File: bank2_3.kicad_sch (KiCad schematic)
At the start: 1 part, among them U1 ECP5-BGA256

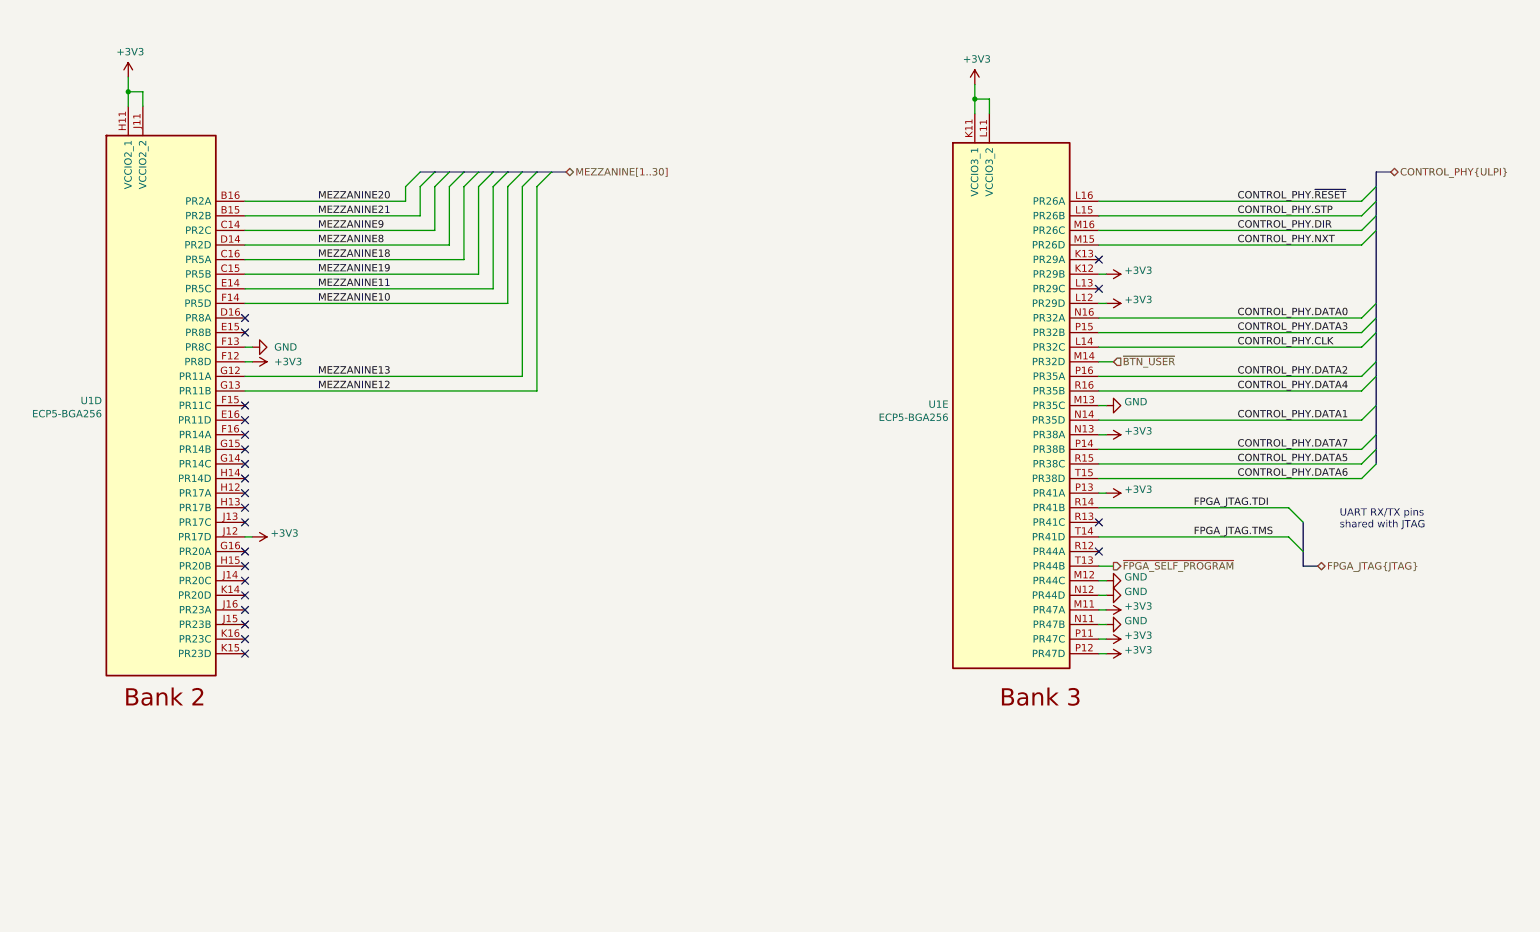
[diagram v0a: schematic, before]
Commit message: Add radio transceiver
Remove Cynthion-specific features
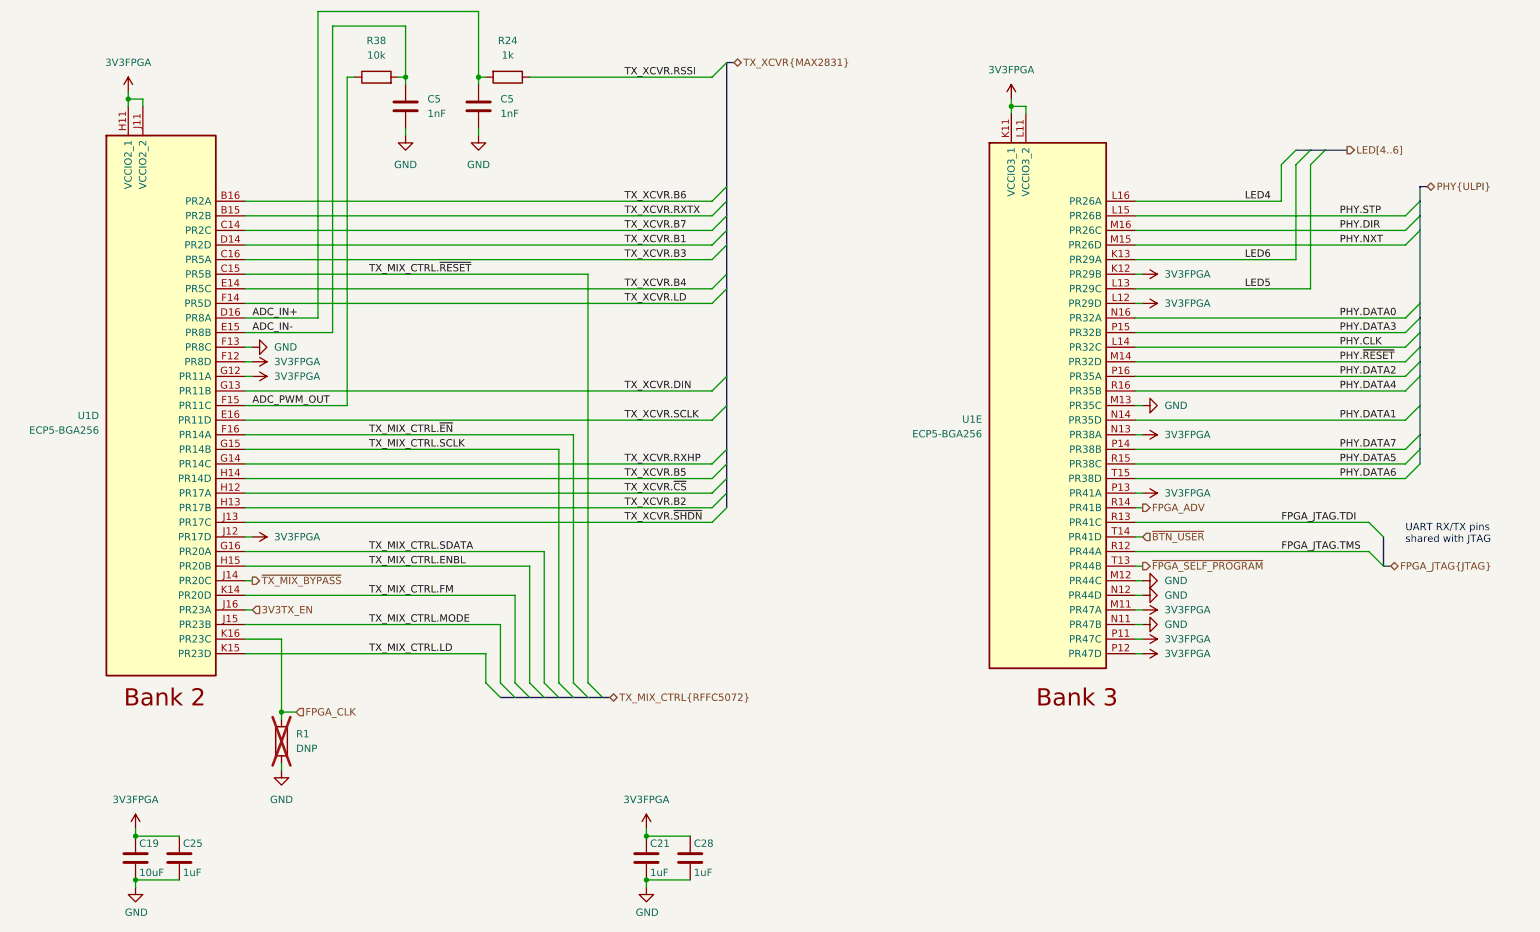
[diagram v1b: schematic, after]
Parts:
- added C19: 10uF, Capacitor_SMD:C_0603_1608Metric, symbol Device:C
- added C21, C25, C28: 1uF, Capacitor_SMD:C_0402_1005Metric, symbol Device:C
- added C5 (x2): 1nF, Capacitor_SMD:C_0201_0603Metric, symbol Device:C
- added R1: DNP, Resistor_SMD:R_0402_1005Metric, symbol Device:R
- added R24: 1k, Resistor_SMD:R_0402_1005Metric, symbol Device:R
- added R38: 10k, Resistor_SMD:R_0402_1005Metric, symbol Device:R
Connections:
- net MEZZANINE13 is gone; now on net 3V3FPGA: U1.G12 (PR11A)
- net FPGA_JTAG.TDI: now also U1.R13 (PR41C); no longer U1.R14 (PR41B)
- net FPGA_JTAG.TMS: now also U1.R12 (PR44A); no longer U1.T14 (PR41D)
- net GND: now also C19.2, C21.2, C25.2, C28.2, C5.2, C5.2, R1.2
- net ~{BTN_USER}: now also U1.T14 (PR41D); no longer U1.M14 (PR32D)
- net ADC_IN+: now reaches U1.D16 (PR8A)
- net ADC_IN+: now also C5.1, R24.2
- net ADC_IN-: now reaches U1.E15 (PR8B)
- net ADC_IN-: now also C5.1, R38.2
- net TX_XCVR.SCLK: now reaches U1.E16 (PR11D)
- net ADC_PWM_OUT: now reaches U1.F15 (PR11C)
- net ADC_PWM_OUT: now also R38.1
- net TX_MIX_CTRL.~{EN}: now reaches U1.F16 (PR14A)
- net TX_XCVR.RXHP: now reaches U1.G14 (PR14C)
- net TX_MIX_CTRL.SCLK: now reaches U1.G15 (PR14B)
- net TX_MIX_CTRL.SDATA: now reaches U1.G16 (PR20A)
- net TX_XCVR.~{CS}: now reaches U1.H12 (PR17A)
- net TX_XCVR.B2: now reaches U1.H13 (PR17B)
- net TX_XCVR.B5: now reaches U1.H14 (PR14D)
- net TX_MIX_CTRL.ENBL: now reaches U1.H15 (PR20B)
- net TX_XCVR.~{SHDN}: now reaches U1.J13 (PR17C)
- net ~{TX_MIX_BYPASS}: now reaches U1.J14 (PR20C)
- net TX_MIX_CTRL.MODE: now reaches U1.J15 (PR23B)
- net 3V3TX_EN: now reaches U1.J16 (PR23A)
- net TX_MIX_CTRL.FM: now reaches U1.K14 (PR20D)
- net TX_MIX_CTRL.LD: now reaches U1.K15 (PR23D)
- net FPGA_CLK: now reaches U1.K16 (PR23C)
- net FPGA_CLK: now also R1.1
- net LED6: now reaches U1.K13 (PR29A)
- net LED5: now reaches U1.L13 (PR29C)
- net +3V3 renamed 3V3FPGA
- net 3V3FPGA: now also C19.1, C21.1, C25.1, C28.1
- net CONTROL_PHY.CLK renamed PHY.CLK
- net CONTROL_PHY.DATA0 renamed PHY.DATA0
- net CONTROL_PHY.DATA1 renamed PHY.DATA1
- net CONTROL_PHY.DATA2 renamed PHY.DATA2
- net CONTROL_PHY.DATA3 renamed PHY.DATA3
- net CONTROL_PHY.DATA4 renamed PHY.DATA4
- net CONTROL_PHY.DATA5 renamed PHY.DATA5
- net CONTROL_PHY.DATA6 renamed PHY.DATA6
- net CONTROL_PHY.DATA7 renamed PHY.DATA7
- net CONTROL_PHY.DIR renamed PHY.DIR
- net CONTROL_PHY.NXT renamed PHY.NXT
- net CONTROL_PHY.STP renamed PHY.STP
- net CONTROL_PHY.~{RESET} renamed LED4
- net MEZZANINE10 renamed TX_XCVR.LD
- net MEZZANINE11 renamed TX_XCVR.B4
- net MEZZANINE12 renamed TX_XCVR.DIN
- net MEZZANINE18 renamed TX_XCVR.B3
- net MEZZANINE19 renamed TX_MIX_CTRL.~{RESET}
- net MEZZANINE20 renamed TX_XCVR.B6
- net MEZZANINE21 renamed TX_XCVR.RXTX
- net MEZZANINE8 renamed TX_XCVR.B1
- net MEZZANINE9 renamed TX_XCVR.B7
- new net FPGA_ADV: U1.R14 (PR41B)
- new net PHY.~{RESET}: U1.M14 (PR32D)
- new net TX_XCVR.RSSI: R24.1
- no-connect marks 23 -> 0
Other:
- company: Copyright 2023 Great Scott Gadgets -> ${COPYRIGHT}
- title: URTI Mainboard -> ${TITLE}
- moved on the sheet: U1E

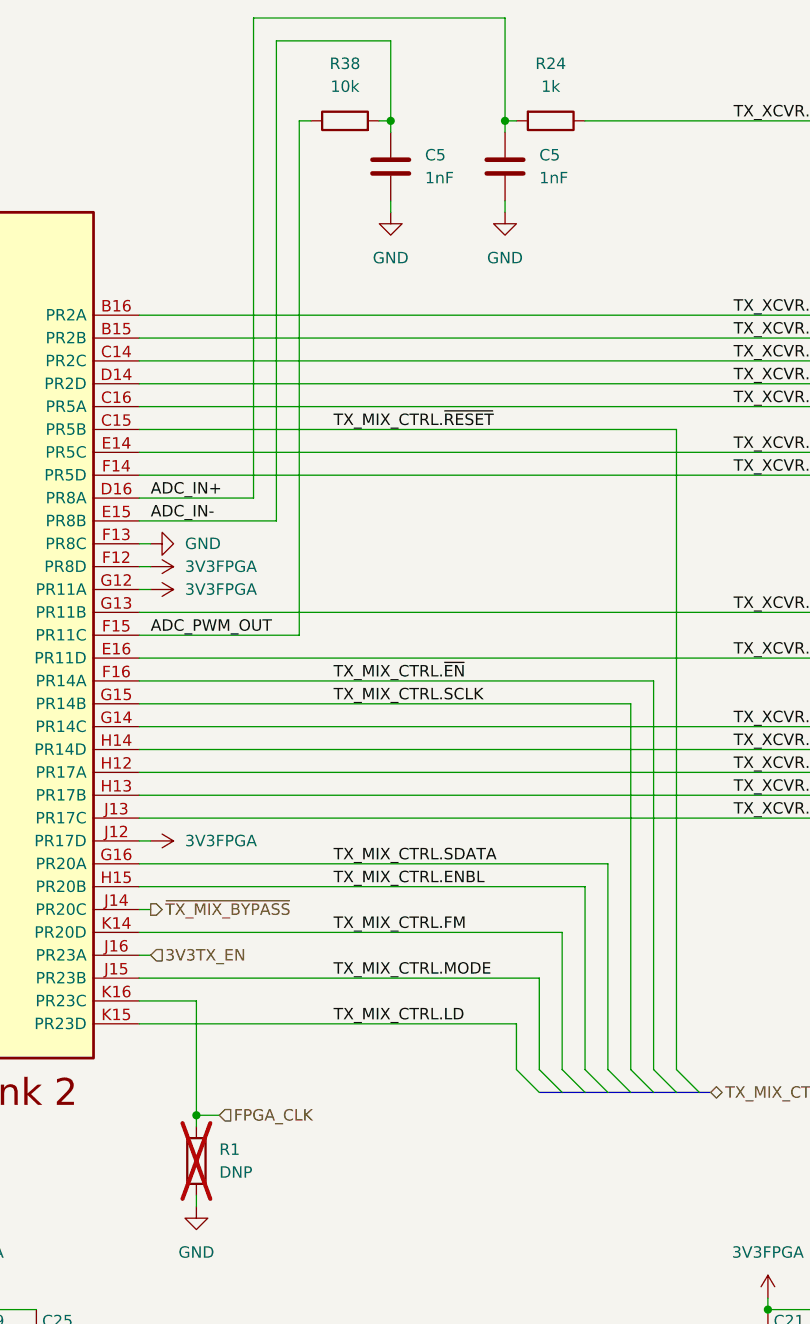
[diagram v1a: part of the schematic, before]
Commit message: Replace open drain clock inverters with push-pull
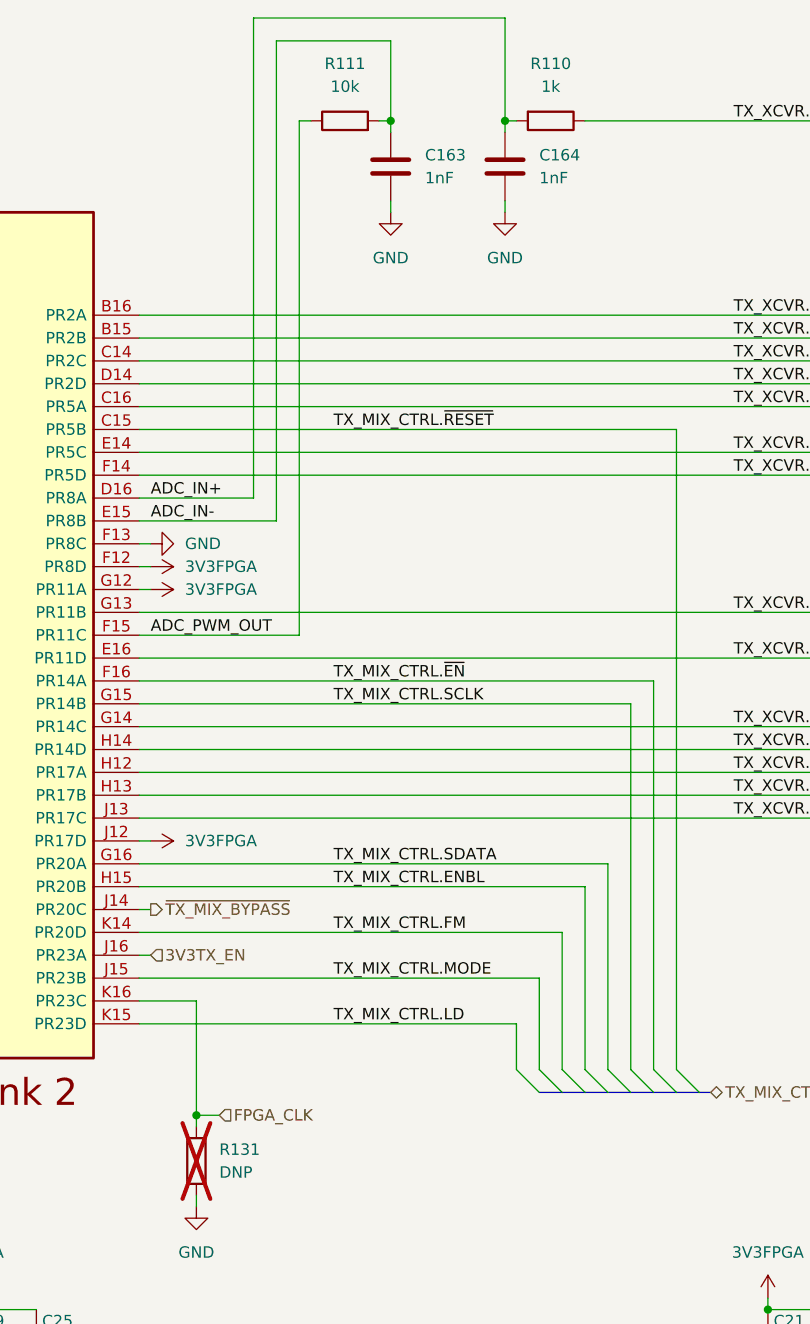
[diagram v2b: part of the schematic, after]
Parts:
- renumbered C5 to C163, C5 to C164, R24 to R110, R38 to R111, R1 to R131
